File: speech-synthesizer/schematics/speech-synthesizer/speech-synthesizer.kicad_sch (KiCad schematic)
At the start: 21 parts, among them Q1 2N4403, Q2 2N4403, U1 74LS245, U2 ATF22V10C, U3 74LS374, U4 74LS374, U5 TMS5220C

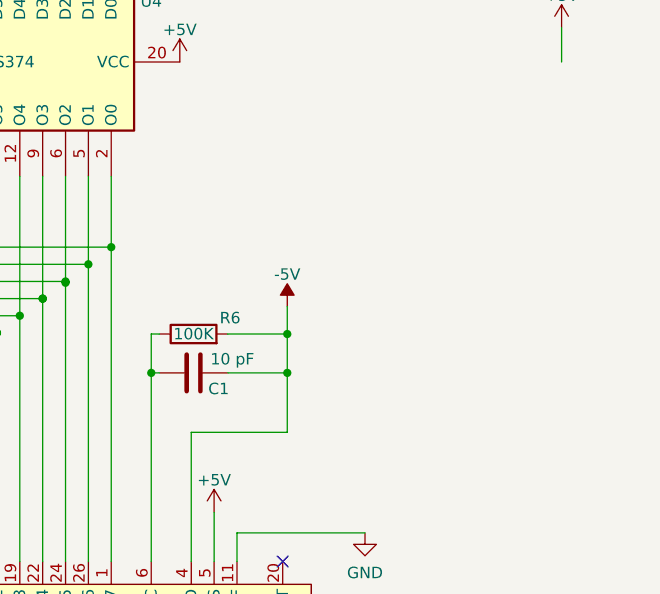
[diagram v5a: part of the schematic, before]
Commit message: improved tms5220 frequency trimming
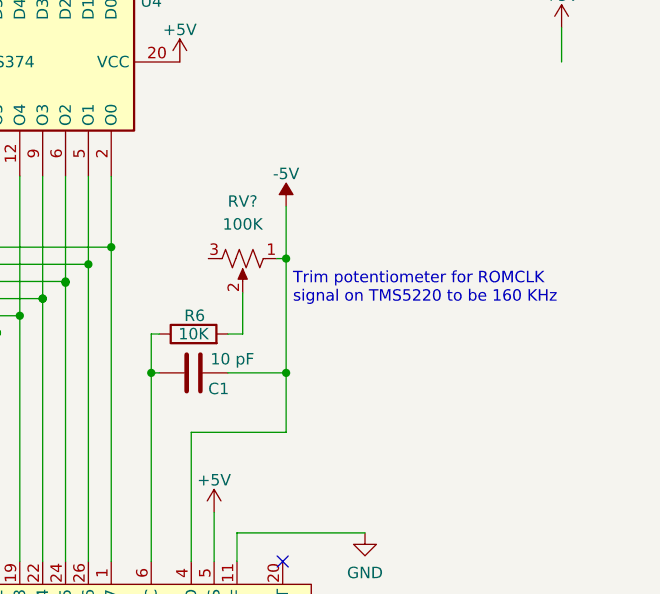
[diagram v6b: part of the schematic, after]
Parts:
- added RV?: 100K, symbol Device:R_Potentiometer_US
- R6: value 100K -> 10K
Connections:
- net -5V: now also RV?.1; no longer R6.2
- new net: R6.2, RV?.2
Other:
- note added: "Trim potentiometer for ROMCLK signal on TMS5220 to be 160 KHz"
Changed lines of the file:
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@@
   (junction (at 75.565 65.405) (diameter 0) (color 0 0 0 0)
   )
+  (junction (at 232.156 82.55) (diameter 0) (color 0 0 0 0)
+  )
   (junction (at 170.307 74.295) (diameter 0) (color 0 0 0 0)
   )
@@
   (junction (at 217.17 82.55) (diameter 0) (color 0 0 0 0)
   )
-  (junction (at 232.283 78.232) (diameter 0) (color 0 0 0 0)
-  )
   (junction (at 172.847 72.39) (diameter 0) (color 0 0 0 0)
   )
@@
   (junction (at 232.791 162.814) (diameter 0) (color 0 0 0 0)
   )
-  (junction (at 232.283 82.55) (diameter 0) (color 0 0 0 0)
+  (junction (at 232.156 69.85) (diameter 0) (color 0 0 0 0)
   )
   (junction (at 55.245 48.006) (diameter 0) (color 0 0 0 0)
@@
     (stroke (width 0) (type default) (color 0 0 0 0))
   )
+  (wire (pts (xy 232.156 64.008) (xy 232.156 69.85))
+    (stroke (width 0) (type default) (color 0 0 0 0))
+  )
   (wire (pts (xy 69.2993 84.582) (xy 80.645 84.582))
     (stroke (width 0) (type default) (color 0 0 0 0))
@@
     (stroke (width 0) (type default) (color 0 0 0 0))
   )
-  (wire (pts (xy 232.283 82.55) (xy 232.283 78.232))
-    (stroke (width 0) (type default) (color 0 0 0 0))
-  )
   (wire (pts (xy 109.728 129.667) (xy 151.13 129.667))
     (stroke (width 0) (type default) (color 0 0 0 0))
@@
     (stroke (width 0) (type default) (color 0 0 0 0))
   )
-  (wire (pts (xy 232.283 78.232) (xy 232.283 75.184))
-    (stroke (width 0) (type default) (color 0 0 0 0))
-  )
   (wire (pts (xy 162.687 80.01) (xy 197.485 80.01))
     (stroke (width 0) (type default) (color 0 0 0 0))
@@
     (stroke (width 0) (type default) (color 0 0 0 0))
   )
+  (wire (pts (xy 232.156 82.55) (xy 232.156 89.154))
+    (stroke (width 0) (type default) (color 0 0 0 0))
+  )
   (wire (pts (xy 78.105 65.405) (xy 85.725 65.405))
     (stroke (width 0) (type default) (color 0 0 0 0))
@@
     (stroke (width 0) (type default) (color 0 0 0 0))
   )
+  (wire (pts (xy 232.156 69.85) (xy 232.156 82.55))
+    (stroke (width 0) (type default) (color 0 0 0 0))
+  )
   (bus (pts (xy 85.725 22.987) (xy 120.269 22.987))
     (stroke (width 0) (type default) (color 0 0 0 0))
@@
     (stroke (width 0) (type default) (color 0 0 0 0))
   )
+  (wire (pts (xy 231.14 69.85) (xy 232.156 69.85))
+    (stroke (width 0) (type default) (color 0 0 0 0))
+  )
   (wire (pts (xy 153.67 132.207) (xy 153.67 26.67))
     (stroke (width 0) (type default) (color 0 0 0 0))
@@
     (stroke (width 0) (type default) (color 0 0 0 0))
   )
+  (wire (pts (xy 227.33 78.232) (xy 227.33 73.66))
+    (stroke (width 0) (type default) (color 0 0 0 0))
+  )
   (bus (pts (xy 200.025 22.987) (xy 202.565 22.987))
     (stroke (width 0) (type default) (color 0 0 0 0))
@@
     (stroke (width 0) (type default) (color 0 0 0 0))
   )
-  (wire (pts (xy 225.679 78.232) (xy 232.283 78.232))
-    (stroke (width 0) (type default) (color 0 0 0 0))
-  )
   (wire (pts (xy 80.645 84.582) (xy 80.645 60.706))
     (stroke (width 0) (type default) (color 0 0 0 0))
@@
     (stroke (width 0) (type default) (color 0 0 0 0))
   )
-  (wire (pts (xy 221.615 89.154) (xy 232.283 89.154))
+  (wire (pts (xy 221.615 89.154) (xy 232.156 89.154))
     (stroke (width 0) (type default) (color 0 0 0 0))
   )
@@
     (stroke (width 0) (type default) (color 0 0 0 0))
   )
-  (wire (pts (xy 225.679 82.55) (xy 232.283 82.55))
-    (stroke (width 0) (type default) (color 0 0 0 0))
-  )
   (wire (pts (xy 127.635 142.367) (xy 127.635 100.076))
     (stroke (width 0) (type default) (color 0 0 0 0))
@@
     (stroke (width 0) (type default) (color 0 0 0 0))
   )
-  (wire (pts (xy 232.283 89.154) (xy 232.283 82.55))
-    (stroke (width 0) (type default) (color 0 0 0 0))
-  )
   (wire (pts (xy 66.675 166.497) (xy 66.675 144.907))
     (stroke (width 0) (type default) (color 0 0 0 0))
@@
     (stroke (width 0) (type default) (color 0 0 0 0))
   )
+  (wire (pts (xy 225.679 78.232) (xy 227.33 78.232))
+    (stroke (width 0) (type default) (color 0 0 0 0))
+  )
   (wire (pts (xy 190.5 135.89) (xy 190.5 169.545))
     (stroke (width 0) (type default) (color 0 0 0 0))
@@
     (stroke (width 0) (type default) (color 0 0 0 0))
   )
+  (wire (pts (xy 225.679 82.55) (xy 232.156 82.55))
+    (stroke (width 0) (type default) (color 0 0 0 0))
+  )
   (text "READY Indicator" (at 113.665 199.39 0)
+    (effects (font (size 1.27 1.27)) (justify left bottom))
+  )
+  (text "Trim potentiometer for ROMCLK\nsignal on TMS5220 to be 160 KHz"
+    (at 232.918 74.93 0)
     (effects (font (size 1.27 1.27)) (justify left bottom))
   )
@@
   (symbol (lib_id "Device:R") (at 221.869 78.232 90) (unit 1)
     (in_bom yes) (on_board yes)
-    (property "Reference" "R6" (id 0) (at 225.933 76.454 90))
-    (property "Value" "100K" (id 1) (at 221.869 78.232 90))
+    (property "Reference" "R6" (id 0) (at 221.996 76.2 90))
+    (property "Value" "10K" (id 1) (at 221.869 78.232 90))
     (property "Footprint" "" (id 2) (at 221.869 80.01 90)
       (effects (font (size 1.27 1.27)) hide)
@@
     (pin "9")
   )
-  (symbol (lib_id "power:-5V") (at 232.283 75.184 0) (unit 1)
-    (in_bom yes) (on_board yes) (fields_autoplaced)
-    (property "Reference" "#PWR015" (id 0) (at 232.283 72.644 0)
-      (effects (font (size 1.27 1.27)) hide)
-    )
-    (property "Value" "-5V" (id 1) (at 232.283 71.6082 0))
-    (property "Footprint" "" (id 2) (at 232.283 75.184 0)
-      (effects (font (size 1.27 1.27)) hide)
-    )
-    (property "Datasheet" "" (id 3) (at 232.283 75.184 0)
+  (symbol (lib_id "power:-5V") (at 232.156 64.008 0) (unit 1)
+    (in_bom yes) (on_board yes) (fields_autoplaced)
+    (property "Reference" "#PWR015" (id 0) (at 232.156 61.468 0)
+      (effects (font (size 1.27 1.27)) hide)
+    )
+    (property "Value" "-5V" (id 1) (at 232.156 60.4322 0))
+    (property "Footprint" "" (id 2) (at 232.156 64.008 0)
+      (effects (font (size 1.27 1.27)) hide)
+    )
+    (property "Datasheet" "" (id 3) (at 232.156 64.008 0)
       (effects (font (size 1.27 1.27)) hide)
     )
@@
     (pin "2")
   )
+  (symbol (lib_id "Device:R_Potentiometer_US") (at 227.33 69.85 270) (unit 1)
+    (in_bom yes) (on_board yes) (fields_autoplaced)
+    (property "Reference" "RV?" (id 0) (at 227.33 63.5 90))
+    (property "Value" "100K" (id 1) (at 227.33 66.04 90))
+    (property "Footprint" "" (id 2) (at 227.33 69.85 0)
+      (effects (font (size 1.27 1.27)) hide)
+    )
+    (property "Datasheet" "~" (id 3) (at 227.33 69.85 0)
+      (effects (font (size 1.27 1.27)) hide)
+    )
+    (pin "1")
+    (pin "2")
+    (pin "3")
+  )
   (symbol (lib_id "Device:R") (at 143.995 149.9579 90) (unit 1)
     (in_bom yes) (on_board yes)
@@
     )
     (path "/4c8624de-33b8-44b9-995d-0810c60b207a"
-      (reference "R6") (unit 1) (value "100K") (footprint "")
+      (reference "R6") (unit 1) (value "10K") (footprint "")
     )
     (path "/683d1e7f-765c-465b-ac2b-ba51df90d511"
@@
       (reference "RN1") (unit 1) (value "10K") (footprint "Resistor_THT:R_Array_SIP9")
     )
+    (path "/ec20a4d2-8a96-482e-a9a1-60f43d105410"
+      (reference "RV?") (unit 1) (value "100K") (footprint "")
+    )
     (path "/1311717c-35fe-41b0-ad8f-751c99efa809"

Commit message: work on speech
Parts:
- added R?: 10K, symbol Device:R
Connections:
- net +5V: now also R?.2
- net at U5.21 (ADD8/DATA): now also R?.1
- no-connect marks 14 -> 13
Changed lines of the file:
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@@
   (no_connect (at 203.2 133.35))
   (no_connect (at 205.74 133.35))
-  (no_connect (at 208.28 133.35))
   (no_connect (at 212.725 133.35))
   (no_connect (at 194.31 133.35))
@@
     (stroke (width 0) (type default) (color 0 0 0 0))
   )
+  (wire (pts (xy 203.2 145.415) (xy 208.28 145.415))
+    (stroke (width 0) (type default) (color 0 0 0 0))
+  )
   (wire (pts (xy 95.885 44.196) (xy 95.885 48.006))
     (stroke (width 0) (type default) (color 0 0 0 0))
@@
     (stroke (width 0) (type default) (color 0 0 0 0))
   )
+  (wire (pts (xy 208.28 133.35) (xy 208.28 137.795))
+    (stroke (width 0) (type default) (color 0 0 0 0))
+  )
   (wire (pts (xy 190.5 135.89) (xy 190.5 169.545))
     (stroke (width 0) (type default) (color 0 0 0 0))
@@
   )
   (wire (pts (xy 167.767 65.151) (xy 167.767 76.2))
-    (stroke (width 0) (type default) (color 0 0 0 0))
-  )
-  (wire (pts (xy 262.763 44.196) (xy 262.763 48.006))
     (stroke (width 0) (type default) (color 0 0 0 0))
   )
@@
   (hierarchical_label "A1" (shape input) (at 40.64 137.287 180)
     (effects (font (size 1.27 1.27)) (justify right))
-  )
-  (symbol (lib_id "power:+5V") (at 262.763 44.196 0) (unit 1)
-    (in_bom yes) (on_board yes) (fields_autoplaced)
-    (property "Reference" "#PWR018" (id 0) (at 262.763 48.006 0)
-      (effects (font (size 1.27 1.27)) hide)
-    )
-    (property "Value" "+5V" (id 1) (at 262.763 40.6202 0))
-    (property "Footprint" "" (id 2) (at 262.763 44.196 0)
-      (effects (font (size 1.27 1.27)) hide)
-    )
-    (property "Datasheet" "" (id 3) (at 262.763 44.196 0)
-      (effects (font (size 1.27 1.27)) hide)
-    )
-    (pin "1")
   )
   (symbol (lib_id "power:+5V") (at 148.209 48.006 0) (unit 1)
@@
     (pin "1")
   )
+  (symbol (lib_id "Device:R") (at 208.28 141.605 0) (unit 1)
+    (in_bom yes) (on_board yes) (fields_autoplaced)
+    (property "Reference" "R?" (id 0) (at 210.058 140.7703 0)
+      (effects (font (size 1.27 1.27)) (justify left))
+    )
+    (property "Value" "10K" (id 1) (at 210.058 143.3072 0)
+      (effects (font (size 1.27 1.27)) (justify left))
+    )
+    (property "Footprint" "" (id 2) (at 206.502 141.605 90)
+      (effects (font (size 1.27 1.27)) hide)
+    )
+    (property "Datasheet" "~" (id 3) (at 208.28 141.605 0)
+      (effects (font (size 1.27 1.27)) hide)
+    )
+    (pin "1")
+    (pin "2")
+  )
   (symbol (lib_id "74xx:74LS374") (at 200.025 48.006 270) (unit 1)
     (in_bom yes) (on_board yes)
@@
     (pin "2")
     (pin "3")
+  )
+  (symbol (lib_id "power:+5V") (at 203.2 145.415 0) (unit 1)
+    (in_bom yes) (on_board yes) (fields_autoplaced)
+    (property "Reference" "#PWR?" (id 0) (at 203.2 149.225 0)
+      (effects (font (size 1.27 1.27)) hide)
+    )
+    (property "Value" "+5V" (id 1) (at 203.2 141.8392 0))
+    (property "Footprint" "" (id 2) (at 203.2 145.415 0)
+      (effects (font (size 1.27 1.27)) hide)
+    )
+    (property "Datasheet" "" (id 3) (at 203.2 145.415 0)
+      (effects (font (size 1.27 1.27)) hide)
+    )
+    (pin "1")
   )
   (symbol (lib_id "power:GND") (at 107.569 50.292 0) (unit 1)
@@
       (reference "#PWR017") (unit 1) (value "GND") (footprint "")
     )
-    (path "/05841a23-93b1-4f56-bbf0-0906326340ae"
-      (reference "#PWR018") (unit 1) (value "+5V") (footprint "")
+    (path "/d906d085-60de-4fe5-a0f9-bb7ee06f2041"
+      (reference "#PWR?") (unit 1) (value "+5V") (footprint "")
     )
     (path "/64016262-4a58-4633-8c0b-d1ca0de4fa44"
@@
       (reference "R7") (unit 1) (value "1.8K") (footprint "")
     )
+    (path "/c40836ab-a0de-4829-b336-937924c1db09"
+      (reference "R?") (unit 1) (value "10K") (footprint "")
+    )
     (path "/976e3de9-e264-4210-9879-e718cd3d6dc2"
